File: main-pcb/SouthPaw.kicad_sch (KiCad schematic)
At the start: 51 parts, among them SW1 SW_Push, SW10 SW_Push, SW11 SW_Push, SW12 SW_Push, SW13 SW_Push, SW14 SW_Push, SW15 SW_Push, SW16 SW_Push, SW17 SW_Push, SW18 SW_Push, SW19 SW_Push, SW2 SW_Push, SW20 SW_Push, SW21 SW_Push, SW22 SW_Push, SW3 SW_Push, SW4 SW_Push, SW5 SW_Push, SW6 SW_Push, SW7 SW_Push, SW8 SW_Push, SW9 SW_Push, U1 KB2040

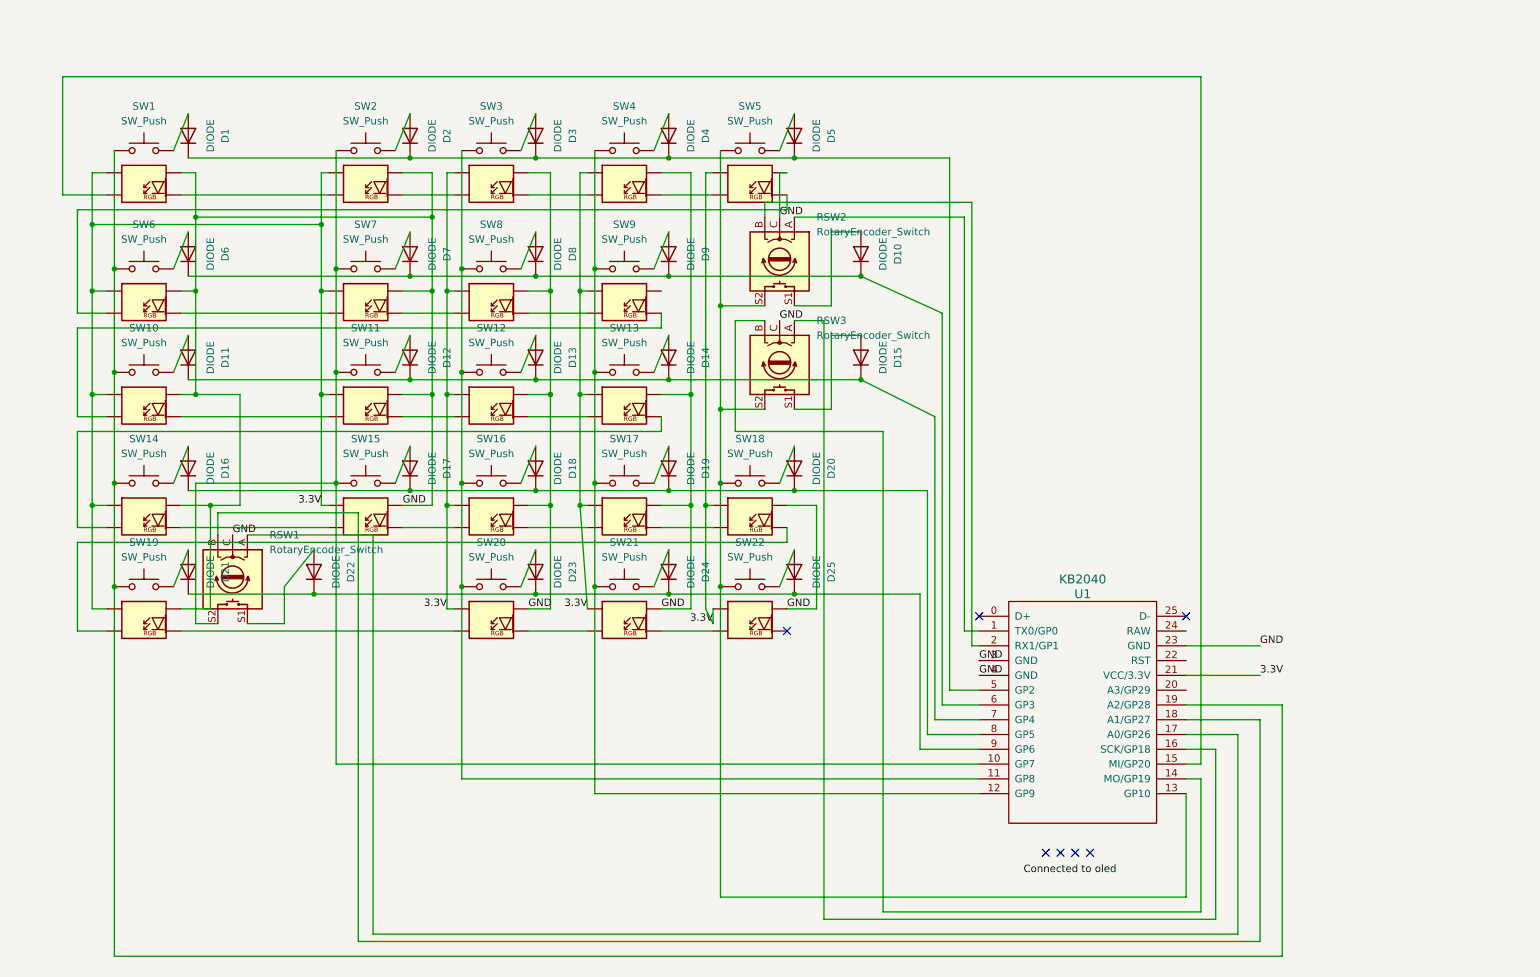
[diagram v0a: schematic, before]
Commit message: fixed pinnouts
rotary encoders now all share a common a pin
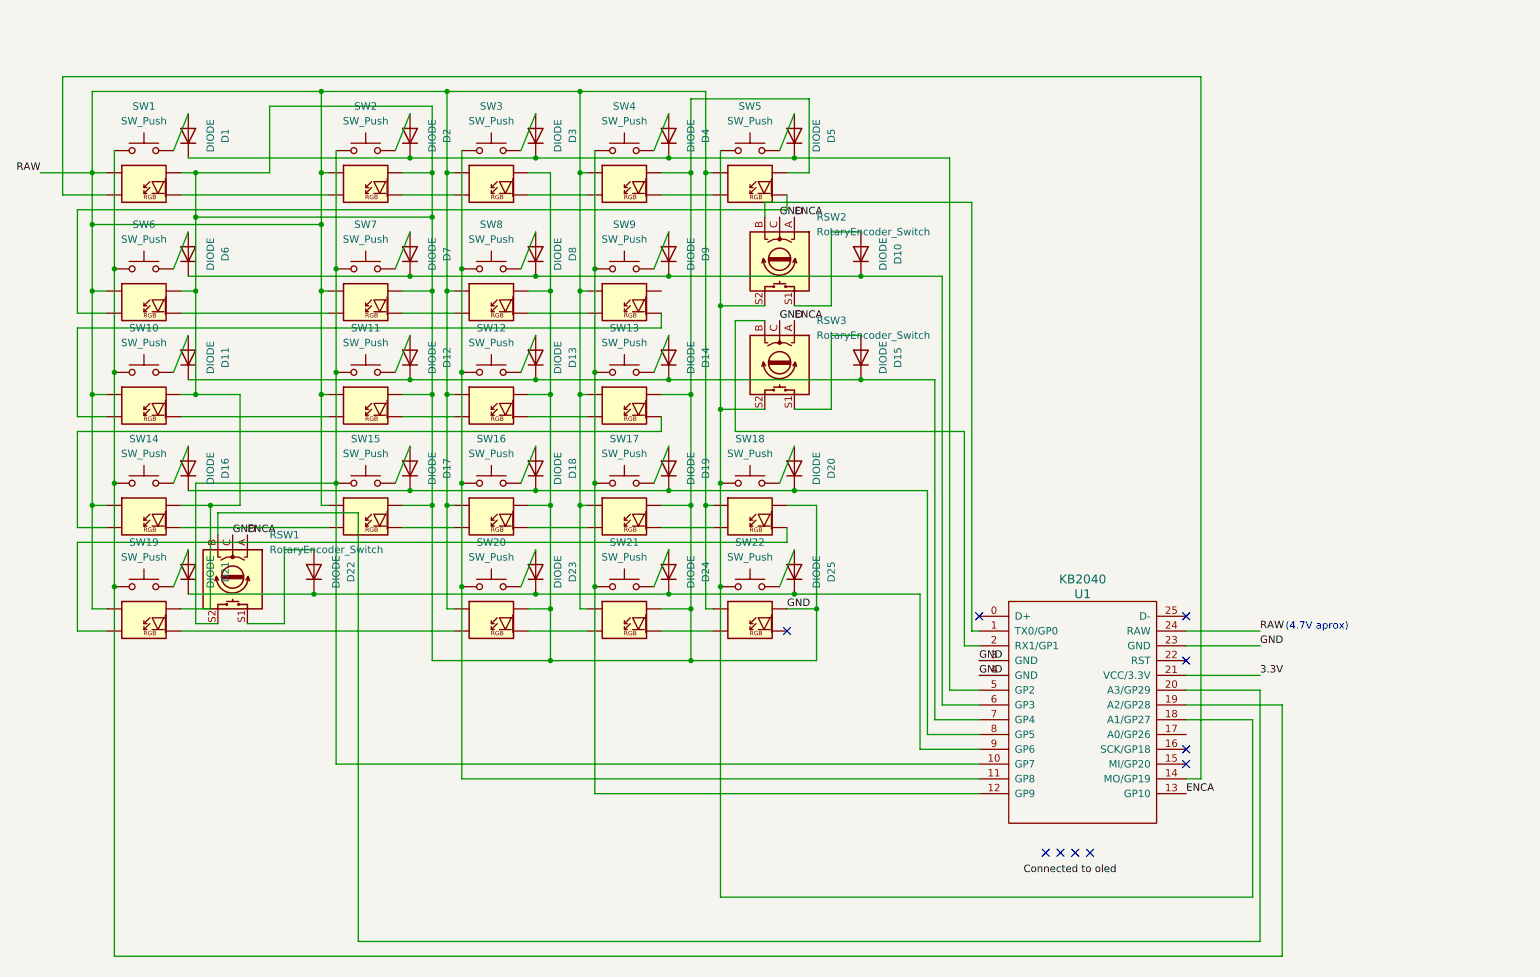
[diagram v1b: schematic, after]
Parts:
- U1: footprint PeteCB:KB2040 through hole hybrid (modified from Elite-C-castellated-24pin-holes) -> PeteCB:KB2040 through hole only (top mount with hotpins 3d model view)
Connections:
- net 3.3V: no longer SW1.21 (ledVDD), SW10.21 (ledVDD), SW11.21 (ledVDD), SW12.21 (ledVDD), SW13.21 (ledVDD), SW14.21 (ledVDD), SW15.21 (ledVDD), SW16.21 (ledVDD), SW17.21 (ledVDD), SW18.21 (ledVDD), SW19.21 (ledVDD), SW2.21 (ledVDD), SW20.21 (ledVDD), SW21.21 (ledVDD), SW22.21 (ledVDD), SW3.21 (ledVDD), SW4.21 (ledVDD), SW5.21 (ledVDD), SW6.21 (ledVDD), SW7.21 (ledVDD), SW8.21 (ledVDD), SW9.21 (ledVDD)
- net at U1.16 (SCK/GP18): no longer RSW3.A
- net at RSW3.B: now also U1.2 (RX1/GP1); no longer U1.14 (MO/GP19)
- net at RSW2.S2, RSW3.S2, SW18.11 (sw1)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: now also U1.18 (A1/GP27); no longer U1.13 (GP10)
- net at U1.1 (TX0/GP0): now also RSW2.B; no longer RSW2.A
- net at SW1.24 (ledDIN): now also U1.14 (MO/GP19); no longer U1.15 (MI/GP20)
- net at U1.17 (A0/GP26): no longer RSW1.A
- net at RSW1.B: now also U1.20 (A3/GP29); no longer U1.18 (A1/GP27)
- net RAW: now reaches U1.24 (RAW)
- net RAW: now also SW1.21 (ledVDD), SW10.21 (ledVDD), SW11.21 (ledVDD), SW12.21 (ledVDD), SW13.21 (ledVDD), SW14.21 (ledVDD), SW15.21 (ledVDD), SW16.21 (ledVDD), SW17.21 (ledVDD), SW18.21 (ledVDD), SW19.21 (ledVDD), SW2.21 (ledVDD), SW20.21 (ledVDD), SW21.21 (ledVDD), SW22.21 (ledVDD), SW3.21 (ledVDD), SW4.21 (ledVDD), SW5.21 (ledVDD), SW6.21 (ledVDD), SW7.21 (ledVDD), SW8.21 (ledVDD), SW9.21 (ledVDD)
- new net ENCA: RSW1.A, RSW2.A, RSW3.A, U1.13 (GP10)
- no-connect marks 7 -> 10
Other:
- note added: "(4.7V aprox)"

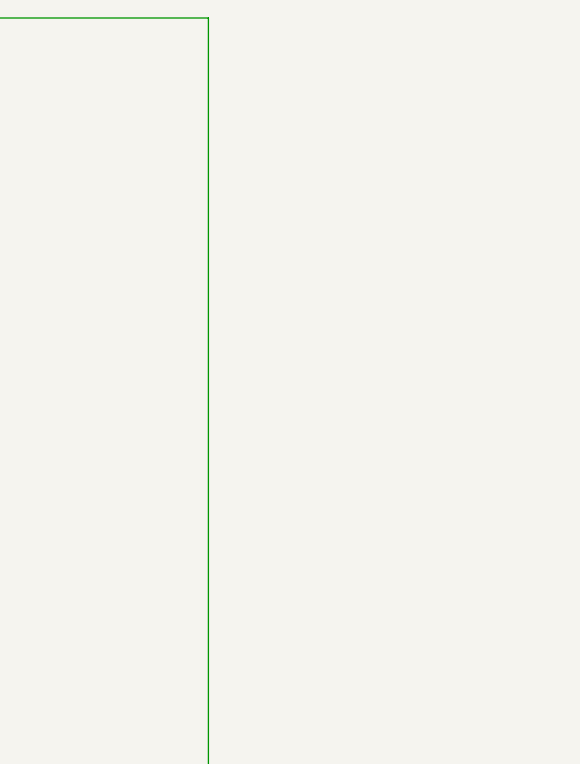
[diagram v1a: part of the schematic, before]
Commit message: Some work on traces (drc errors present)
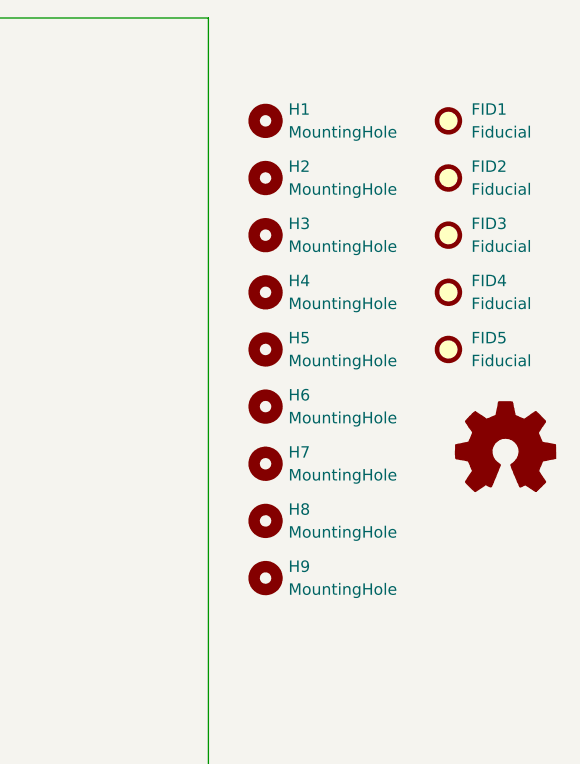
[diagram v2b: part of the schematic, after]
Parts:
- added FID1, FID2, FID3, FID4, FID5: Fiducial, Fiducial:Fiducial_0.5mm_Mask1mm, symbol Mechanical:Fiducial
- added H1: MountingHole, PeteCB:0.91in 128x32 I2C STEMMA QT standoff only with cutout, symbol Mechanical:MountingHole
- added H2, H3, H4, H5, H6, H7, H8, H9: MountingHole, PeteCB:m2.5 hole, symbol Mechanical:MountingHole
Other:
- company: (none) -> PeteCB
- title: (none) -> SouthPaw

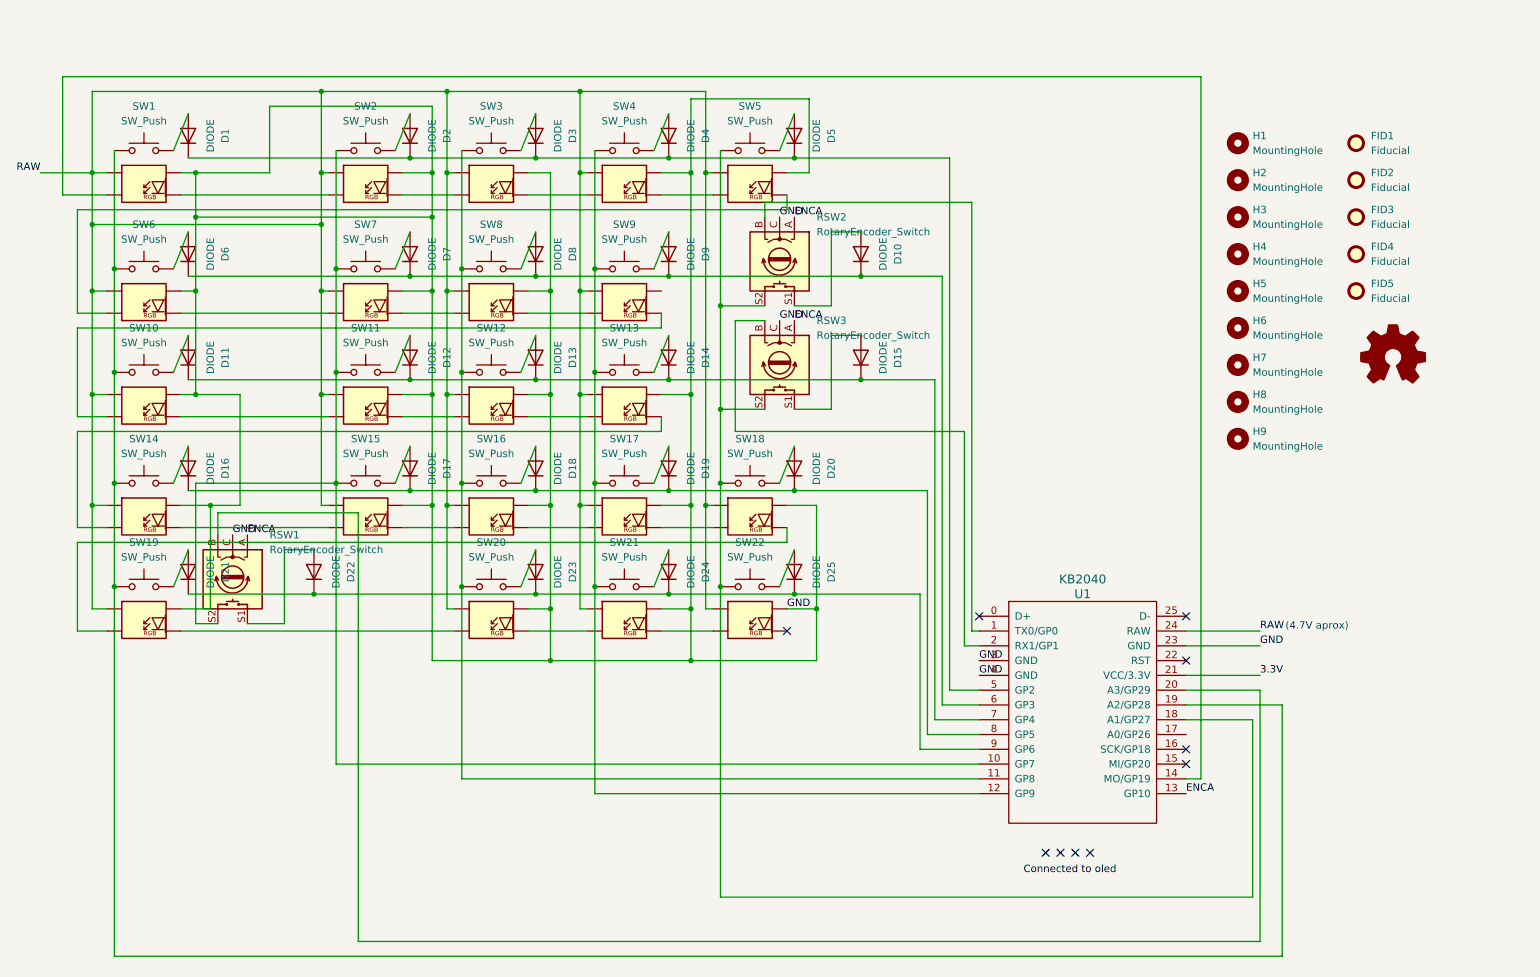
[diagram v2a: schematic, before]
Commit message: fixed schematic errors
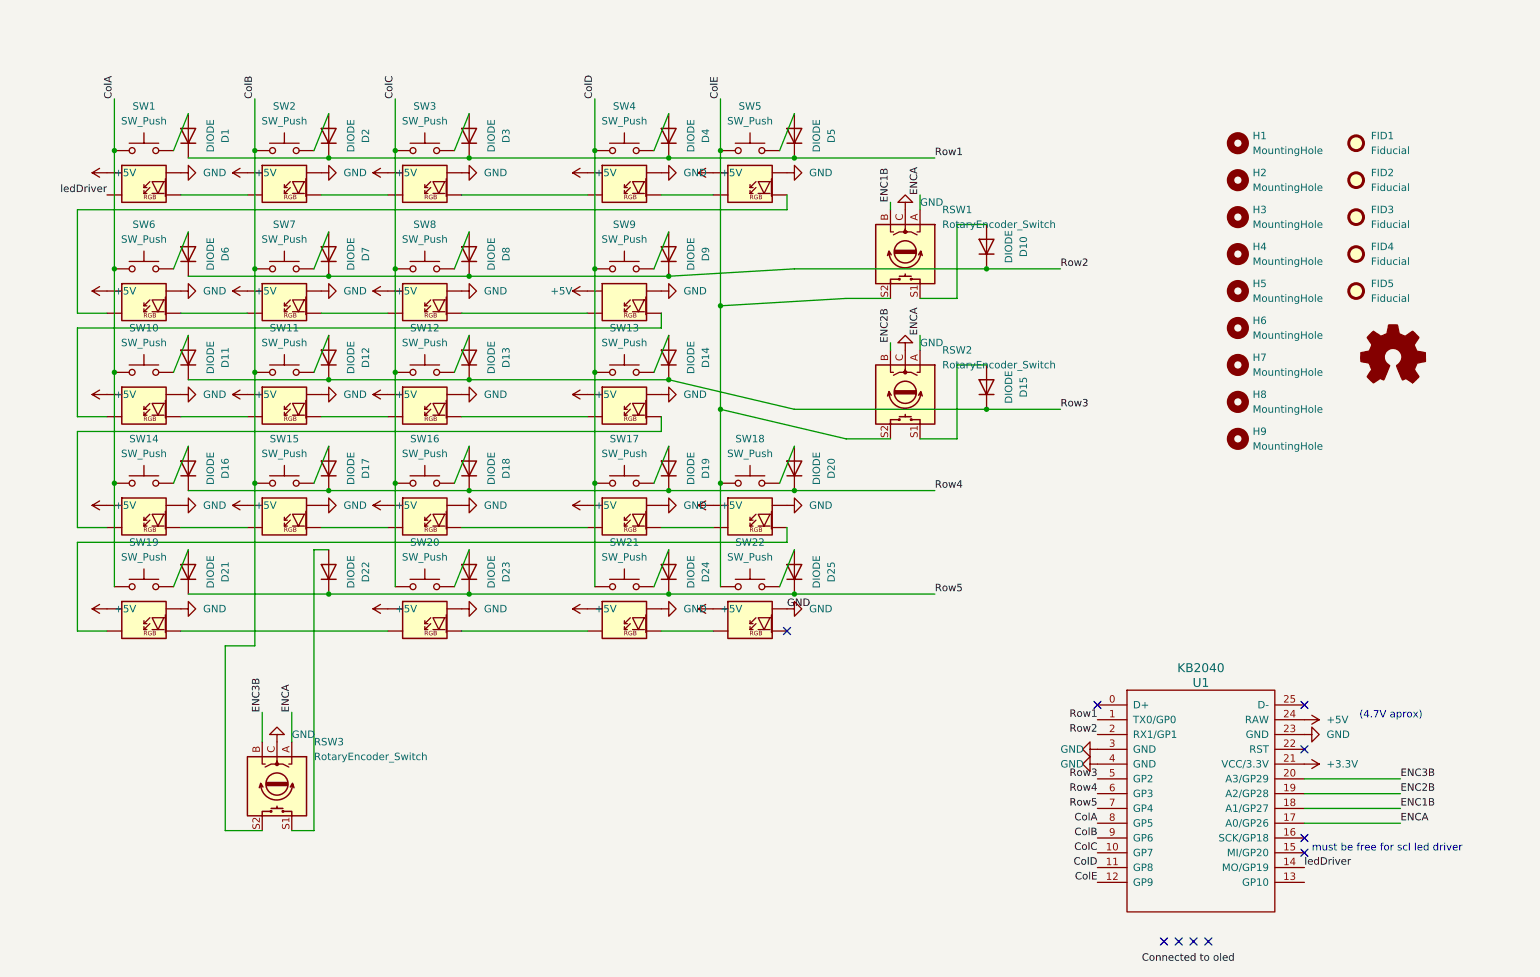
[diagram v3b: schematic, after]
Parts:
- renumbered RSW2 to RSW1, RSW3 to RSW2, RSW1 to RSW3
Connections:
- net ENCA: now also U1.17 (A0/GP26); no longer U1.13 (GP10)
- net GND: now also SW9.23 (ledGND)
- net Row2: now reaches D10.2 (K), D6.2 (K), D7.2 (K), D8.2 (K), D9.2 (K)
- net Row2: now also U1.2 (RX1/GP1); no longer U1.6 (GP3)
- net Row5: now reaches D21.2 (K), D22.2 (K), D23.2 (K), D24.2 (K), D25.2 (K)
- net Row5: now also U1.7 (GP4); no longer U1.9 (GP6)
- net ENC2B: now reaches RSW2.B
- net ENC2B: now also U1.19 (A2/GP28); no longer U1.2 (RX1/GP1)
- net ColE: now reaches RSW1.S2, RSW2.S2, SW18.11 (sw1), SW22.11 (sw1), SW5.11 (sw1)
- net ColE: now also U1.12 (GP9); no longer U1.18 (A1/GP27)
- net ColC: now reaches SW12.11 (sw1), SW16.11 (sw1), SW20.11 (sw1), SW3.11 (sw1), SW8.11 (sw1)
- net ColC: now also U1.10 (GP7); no longer U1.11 (GP8)
- net ColB: now reaches RSW3.S2, SW11.11 (sw1), SW15.11 (sw1), SW2.11 (sw1), SW7.11 (sw1)
- net ColB: now also U1.9 (GP6); no longer U1.10 (GP7)
- net Row3: now reaches D11.2 (K), D12.2 (K), D13.2 (K), D14.2 (K), D15.2 (K)
- net Row3: now also U1.5 (GP2); no longer U1.7 (GP4)
- net Row1: now reaches D1.2 (K), D2.2 (K), D3.2 (K), D4.2 (K), D5.2 (K)
- net Row1: now also U1.1 (TX0/GP0); no longer U1.5 (GP2)
- net Row4: now reaches D16.2 (K), D17.2 (K), D18.2 (K), D19.2 (K), D20.2 (K)
- net Row4: now also U1.6 (GP3); no longer U1.8 (GP5)
- net ColD: now reaches SW13.11 (sw1), SW17.11 (sw1), SW21.11 (sw1), SW4.11 (sw1), SW9.11 (sw1)
- net ColD: now also U1.11 (GP8); no longer U1.12 (GP9)
- net ENC1B: now reaches RSW1.B
- net ENC1B: now also U1.18 (A1/GP27); no longer U1.1 (TX0/GP0)
- net ColA: now reaches SW1.11 (sw1), SW10.11 (sw1), SW14.11 (sw1), SW19.11 (sw1), SW6.11 (sw1)
- net ColA: now also U1.8 (GP5); no longer U1.19 (A2/GP28)
- net ledDriver: now reaches SW1.24 (ledDIN), U1.14 (MO/GP19)
- net ENC3B: now reaches RSW3.B, U1.20 (A3/GP29)
- net 3.3V renamed +3.3V
- net RAW renamed +5V
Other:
- note added: "must be free for scl led driver"
- moved on the sheet: D10, D12, D13, D15, D17, D18, D2, D22, D23, D3, D7, D8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

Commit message: routing underway
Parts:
- added JPSH1: Jumper_3_Open, Jumper:SolderJumper-3_P2.0mm_Open_TrianglePad1.0x1.5mm, symbol Jumper:Jumper_3_Open
- added JPSP2, JPSP3: Jumper_2_Open, Jumper:SolderJumper-2_P1.3mm_Open_TrianglePad1.0x1.5mm, symbol Jumper:Jumper_2_Open
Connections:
- net at U1.15 (MI/GP20): now also JPSP3.1 (A)
- net at U1.16 (SCK/GP18): now also JPSP2.1 (A)
- net ENCA renamed ENC1A(sharedInSclLedMode)
- net ENC1A(sharedInSclLedMode): now also JPSH1.1 (A); no longer RSW2.A, RSW3.A
- new net ENC2A: JPSH1.2 (C), JPSP2.2 (B), RSW2.A
- new net ENC3A: JPSH1.3 (B), JPSP3.2 (B), RSW3.A
- no-connect marks 10 -> 8
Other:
- note added: "Oled Driver Pins From Stema QT Connector"
- note added: "must be unconnected for scl led driver mode"
- note removed: "must be free for scl led driver"
- moved on the sheet: U1

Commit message: I think Im finished with es2
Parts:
- added H10, H11: MountingHole, PeteCB:m2.5 hole, symbol Mechanical:MountingHole
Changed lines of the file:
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@@
     (pin "1")
+  )
+  (symbol (lib_id "Mechanical:MountingHole") (at 237.49 90.17 0) (unit 1)
+    (in_bom no) (on_board yes) (fields_autoplaced)
+    (property "Reference" "H11" (id 0) (at 240.03 88.8999 0)
+      (effects (font (size 1.27 1.27)) (justify left))
+    )
+    (property "Value" "MountingHole" (id 1) (at 240.03 91.4399 0)
+      (effects (font (size 1.27 1.27)) (justify left))
+    )
+    (property "Footprint" "PeteCB:m2.5 hole" (id 2) (at 237.49 90.17 0)
+      (effects (font (size 1.27 1.27)) hide)
+    )
+    (property "Datasheet" "~" (id 3) (at 237.49 90.17 0)
+      (effects (font (size 1.27 1.27)) hide)
+    )
   )
   (symbol (lib_id "power:+5V") (at 67.31 67.31 90) (unit 1)
@@
     )
   )
+  (symbol (lib_id "Mechanical:MountingHole") (at 237.49 83.82 0) (unit 1)
+    (in_bom no) (on_board yes) (fields_autoplaced)
+    (property "Reference" "H10" (id 0) (at 240.03 82.5499 0)
+      (effects (font (size 1.27 1.27)) (justify left))
+    )
+    (property "Value" "MountingHole" (id 1) (at 240.03 85.0899 0)
+      (effects (font (size 1.27 1.27)) (justify left))
+    )
+    (property "Footprint" "PeteCB:m2.5 hole" (id 2) (at 237.49 83.82 0)
+      (effects (font (size 1.27 1.27)) hide)
+    )
+    (property "Datasheet" "~" (id 3) (at 237.49 83.82 0)
+      (effects (font (size 1.27 1.27)) hide)
+    )
+  )
   (symbol (lib_id "power:+5V") (at 67.31 86.36 90) (unit 1)
     (in_bom yes) (on_board yes) (fields_autoplaced)
@@
       (reference "H9") (unit 1) (value "MountingHole") (footprint "PeteCB:m2.5 hole")
     )
+    (path "/ec986475-6741-4668-85db-2e84b215487c"
+      (reference "H10") (unit 1) (value "MountingHole") (footprint "PeteCB:m2.5 hole")
+    )
+    (path "/e54635e3-39eb-4d20-946b-c10a0a729bce"
+      (reference "H11") (unit 1) (value "MountingHole") (footprint "PeteCB:m2.5 hole")
+    )
     (path "/03895599-3e03-4cb1-a00d-fcf3143cc021"
